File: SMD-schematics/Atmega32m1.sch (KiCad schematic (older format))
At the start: 33 parts, among them J11 Conn_02x06_Odd_Even, J12 Conn_02x06_Odd_Even, J7 Conn_02x06_Odd_Even, J8 Conn_02x06_Odd_Even, J9 DB9_Female, SW1 SW_Push_Dual, SW2 SW_Push_Dual, SW3 SW_Push_Dual, U5 MAX232, Y2 16Mhz

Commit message: "placing the footprints in PCB design no trakes yet"
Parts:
- JP5: renamed from JP?; footprint (none) -> Pin_Headers:Pin_Header_Straight_1x02_Pitch2.54mm
- U2: renamed from U?; footprint TQFP32 -> Housings_QFP:TQFP-32_7x7mm_Pitch0.8mm
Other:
- moved on the sheet: C10, C12, C13, C14, U5
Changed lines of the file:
@@
 L MAX232 U5
 U 1 1 59EBF4CD
-P 8600 3350
-F 0 "U5" H 8500 4475 50  0000 R CNN
-F 1 "MAX232" H 8500 4400 50  0000 R CNN
-F 2 "Housings_SOIC:SOIC-16_3.9x9.9mm_Pitch1.27mm" H 8650 2300 50  0001 L CNN
-F 3 "" H 8600 3450 50  0001 C CNN
-	1    8600 3350
+P 8450 3400
+F 0 "U5" H 8350 4525 50  0000 R CNN
+F 1 "MAX232" H 8350 4450 50  0000 R CNN
+F 2 "Housings_SOIC:SOIC-16_3.9x9.9mm_Pitch1.27mm" H 8500 2350 50  0001 L CNN
+F 3 "" H 8450 3500 50  0001 C CNN
+	1    8450 3400
 	1    0    0    -1
 $EndComp
@@
 L CP C10
 U 1 1 59EBFD51
-P 7350 2850
-F 0 "C10" H 7375 2950 50  0000 L CNN
-F 1 "1uf" H 7375 2750 50  0000 L CNN
-F 2 "Capacitors_SMD:CP_Elec_8x6.5" H 7388 2700 50  0001 C CNN
-F 3 "" H 7350 2850 50  0001 C CNN
-	1    7350 2850
+P 7350 2650
+F 0 "C10" H 7375 2750 50  0000 L CNN
+F 1 "1uf" H 7375 2550 50  0000 L CNN
+F 2 "Capacitors_SMD:CP_Elec_8x6.5" H 7388 2500 50  0001 C CNN
+F 3 "" H 7350 2650 50  0001 C CNN
+	1    7350 2650
 	1    0    0    -1
 $EndComp
@@
 L CP C12
 U 1 1 59EBFDFB
-P 9700 2850
-F 0 "C12" H 9725 2950 50  0000 L CNN
-F 1 "1uf" H 9725 2750 50  0000 L CNN
-F 2 "Capacitors_SMD:CP_Elec_8x6.5" H 9738 2700 50  0001 C CNN
-F 3 "" H 9700 2850 50  0001 C CNN
-	1    9700 2850
+P 9700 2650
+F 0 "C12" H 9725 2750 50  0000 L CNN
+F 1 "1uf" H 9725 2550 50  0000 L CNN
+F 2 "Capacitors_SMD:CP_Elec_8x6.5" H 9738 2500 50  0001 C CNN
+F 3 "" H 9700 2650 50  0001 C CNN
+	1    9700 2650
 	1    0    0    -1
 $EndComp
@@
 $EndComp
 $Comp
-L GND #PWR016
+L GND #PWR27
 U 1 1 59EBFEF1
 P 8650 2350
-F 0 "#PWR016" H 8650 2100 50  0001 C CNN
+F 0 "#PWR27" H 8650 2100 50  0001 C CNN
 F 1 "GND" H 8650 2200 50  0000 C CNN
 F 2 "" H 8650 2350 50  0001 C CNN
@@
 L CP C13
 U 1 1 59EBFF32
-P 10200 3200
-F 0 "C13" H 10225 3300 50  0000 L CNN
-F 1 "1uf" H 10225 3100 50  0000 L CNN
-F 2 "Capacitors_SMD:CP_Elec_8x6.5" H 10238 3050 50  0001 C CNN
-F 3 "" H 10200 3200 50  0001 C CNN
-	1    10200 3200
+P 10200 3000
+F 0 "C13" H 10225 3100 50  0000 L CNN
+F 1 "1uf" H 10225 2900 50  0000 L CNN
+F 2 "Capacitors_SMD:CP_Elec_8x6.5" H 10238 2850 50  0001 C CNN
+F 3 "" H 10200 3000 50  0001 C CNN
+	1    10200 3000
 	0    -1   -1   0
 $EndComp
@@
 L CP C14
 U 1 1 59EBFFAC
-P 10350 3550
-F 0 "C14" H 10375 3650 50  0000 L CNN
-F 1 "1uf" H 10375 3450 50  0000 L CNN
-F 2 "Capacitors_SMD:CP_Elec_8x6.5" H 10388 3400 50  0001 C CNN
-F 3 "" H 10350 3550 50  0001 C CNN
-	1    10350 3550
+P 10350 3350
+F 0 "C14" H 10375 3450 50  0000 L CNN
+F 1 "1uf" H 10375 3250 50  0000 L CNN
+F 2 "Capacitors_SMD:CP_Elec_8x6.5" H 10388 3200 50  0001 C CNN
+F 3 "" H 10350 3350 50  0001 C CNN
+	1    10350 3350
 	0    1    1    0
 $EndComp
 $Comp
-L GND #PWR017
+L GND #PWR28
 U 1 1 59EBFFE3
-P 10650 3350
-F 0 "#PWR017" H 10650 3100 50  0001 C CNN
-F 1 "GND" H 10650 3200 50  0000 C CNN
-F 2 "" H 10650 3350 50  0001 C CNN
-F 3 "" H 10650 3350 50  0001 C CNN
-	1    10650 3350
+P 10650 3150
+F 0 "#PWR28" H 10650 2900 50  0001 C CNN
+F 1 "GND" H 10650 3000 50  0000 C CNN
+F 2 "" H 10650 3150 50  0001 C CNN
+F 3 "" H 10650 3150 50  0001 C CNN
+	1    10650 3150
 	0    -1   -1   0
 $EndComp
 $Comp
-L GND #PWR018
+L GND #PWR26
 U 1 1 59EC0239
 P 8450 4950
-F 0 "#PWR018" H 8450 4700 50  0001 C CNN
+F 0 "#PWR26" H 8450 4700 50  0001 C CNN
 F 1 "GND" H 8450 4800 50  0000 C CNN
 F 2 "" H 8450 4950 50  0001 C CNN
@@
 $EndComp
 $Comp
-L +5V #PWR019
+L +5V #PWR17
 U 1 1 59EC0C0E
 P 4100 4200
-F 0 "#PWR019" H 4100 4050 50  0001 C CNN
+F 0 "#PWR17" H 4100 4050 50  0001 C CNN
 F 1 "+5V" H 4100 4340 50  0000 C CNN
 F 2 "" H 4100 4200 50  0001 C CNN
@@
 NoConn ~ 10350 5000
 $Comp
-L GND #PWR020
+L GND #PWR18
 U 1 1 5AA2B4DD
 P 4950 4850
-F 0 "#PWR020" H 4950 4600 50  0001 C CNN
+F 0 "#PWR18" H 4950 4600 50  0001 C CNN
 F 1 "GND" H 4950 4700 50  0000 C CNN
 F 2 "" H 4950 4850 50  0001 C CNN
@@
 $EndComp
 $Comp
-L GND #PWR021
+L GND #PWR13
 U 1 1 5AA312D5
 P 700 2150
-F 0 "#PWR021" H 700 1900 50  0001 C CNN
+F 0 "#PWR13" H 700 1900 50  0001 C CNN
 F 1 "GND" H 700 2000 50  0000 C CNN
 F 2 "" H 700 2150 50  0001 C CNN
@@
 $EndComp
 $Comp
-L +5V #PWR022
+L +5V #PWR14
 U 1 1 5AA3500F
 P 850 1250
-F 0 "#PWR022" H 850 1100 50  0001 C CNN
+F 0 "#PWR14" H 850 1100 50  0001 C CNN
 F 1 "+5V" H 850 1390 50  0000 C CNN
 F 2 "" H 850 1250 50  0001 C CNN
@@
 $EndComp
 $Comp
-L GND #PWR023
+L GND #PWR16
 U 1 1 5AA38656
 P 3550 6450
-F 0 "#PWR023" H 3550 6200 50  0001 C CNN
+F 0 "#PWR16" H 3550 6200 50  0001 C CNN
 F 1 "GND" H 3550 6300 50  0000 C CNN
 F 2 "" H 3550 6450 50  0001 C CNN
@@
 $EndComp
 $Comp
-L GND #PWR024
+L GND #PWR15
 U 1 1 5AA3A648
 P 850 4250
-F 0 "#PWR024" H 850 4000 50  0001 C CNN
+F 0 "#PWR15" H 850 4000 50  0001 C CNN
 F 1 "GND" H 850 4100 50  0000 C CNN
 F 2 "" H 850 4250 50  0001 C CNN
@@
 $EndComp
 $Comp
-L +5V #PWR025
+L +5V #PWR19
 U 1 1 5AA5B656
 P 5200 7350
-F 0 "#PWR025" H 5200 7200 50  0001 C CNN
+F 0 "#PWR19" H 5200 7200 50  0001 C CNN
 F 1 "+5V" H 5200 7490 50  0000 C CNN
 F 2 "" H 5200 7350 50  0001 C CNN
@@
 $EndComp
 $Comp
-L +5V #PWR026
+L +5V #PWR22
 U 1 1 5AA5B65C
 P 6000 4150
-F 0 "#PWR026" H 6000 4000 50  0001 C CNN
+F 0 "#PWR22" H 6000 4000 50  0001 C CNN
 F 1 "+5V" H 6000 4290 50  0000 C CNN
 F 2 "" H 6000 4150 50  0001 C CNN
@@
 AT-ADC2
 $Comp
-L GND #PWR027
+L GND #PWR20
 U 1 1 5AA5B91B
 P 5800 5250
-F 0 "#PWR027" H 5800 5000 50  0001 C CNN
+F 0 "#PWR20" H 5800 5000 50  0001 C CNN
 F 1 "GND" H 5800 5100 50  0000 C CNN
 F 2 "" H 5800 5250 50  0001 C CNN
@@
 $EndComp
 $Comp
-L +5V #PWR028
+L +5V #PWR25
 U 1 1 5AA5D9AA
 P 6900 4150
-F 0 "#PWR028" H 6900 4000 50  0001 C CNN
+F 0 "#PWR25" H 6900 4000 50  0001 C CNN
 F 1 "+5V" H 6900 4290 50  0000 C CNN
 F 2 "" H 6900 4150 50  0001 C CNN
@@
 AT-ADC3
 $Comp
-L GND #PWR029
+L GND #PWR21
 U 1 1 5AA6CC67
 P 5950 2900
-F 0 "#PWR029" H 5950 2650 50  0001 C CNN
+F 0 "#PWR21" H 5950 2650 50  0001 C CNN
 F 1 "GND" H 5950 2750 50  0000 C CNN
 F 2 "" H 5950 2900 50  0001 C CNN
@@
 $EndComp
 $Comp
-L GND #PWR030
+L GND #PWR23
 U 1 1 5AA87097
 P 6150 7350
-F 0 "#PWR030" H 6150 7100 50  0001 C CNN
+F 0 "#PWR23" H 6150 7100 50  0001 C CNN
 F 1 "GND" H 6150 7200 50  0000 C CNN
 F 2 "" H 6150 7350 50  0001 C CNN
@@
 $EndComp
 $Comp
-L GND #PWR031
+L GND #PWR24
 U 1 1 5AA88971
 P 6150 7600
-F 0 "#PWR031" H 6150 7350 50  0001 C CNN
+F 0 "#PWR24" H 6150 7350 50  0001 C CNN
 F 1 "GND" H 6150 7450 50  0000 C CNN
 F 2 "" H 6150 7600 50  0001 C CNN
@@
 	8650 2300 8650 2350
 Wire Wire Line
-	9550 3550 10200 3550
-Wire Wire Line
-	9250 3200 10050 3200
-Wire Wire Line
-	10550 3200 10350 3200
-Wire Wire Line
-	10550 3200 10550 3550
-Wire Wire Line
-	10550 3350 10650 3350
-Wire Wire Line
-	10550 3550 10500 3550
-Connection ~ 10550 3350
-Wire Wire Line
-	9250 2700 9700 2700
-Wire Wire Line
-	9700 3000 9250 3000
-Wire Wire Line
-	7650 2700 7350 2700
-Wire Wire Line
-	7350 3000 7650 3000
-Wire Wire Line
-	9550 3550 9550 3500
-Wire Wire Line
-	9550 3500 9250 3500
-Wire Wire Line
-	8450 4800 8450 4950
+	9550 3350 10200 3350
+Wire Wire Line
+	9250 3000 10050 3000
+Wire Wire Line
+	10550 3000 10350 3000
+Wire Wire Line
+	10550 3000 10550 3350
+Wire Wire Line
+	10550 3150 10650 3150
+Wire Wire Line
+	10550 3350 10500 3350
+Connection ~ 10550 3150
+Wire Wire Line
+	9250 2500 9700 2500
+Wire Wire Line
+	9700 2800 9250 2800
+Wire Wire Line
+	7650 2500 7350 2500
+Wire Wire Line
+	7350 2800 7650 2800
+Wire Wire Line
+	9550 3350 9550 3300
+Wire Wire Line
+	9550 3300 9250 3300
 Wire Wire Line
 	10350 4500 9750 4500
@@
 Wire Wire Line
 	9350 4850 8450 4850
-Connection ~ 8450 4850
 Wire Wire Line
 	4950 4850 4850 4850
@@
 ~AT-RST
 $Comp
-L ATMEGA32M1-AU U?
+L ATMEGA32M1-AU U2
 U 1 1 5AC2CAD1
 P 2350 3100
-F 0 "U?" H 1400 4930 50  0000 L BNN
+F 0 "U2" H 1400 4930 50  0000 L BNN
 F 1 "ATMEGA32M1-AU" H 2850 1700 50  0000 L BNN
-F 2 "TQFP32" H 2350 3100 50  0001 C CIN
+F 2 "Housings_QFP:TQFP-32_7x7mm_Pitch0.8mm" H 2350 3100 50  0001 C CIN
 F 3 "" H 2350 3100 50  0001 C CNN
 	1    2350 3100
@@
 SPI-DW
 $Comp
-L Jumper_NO_Small JP?
+L Jumper_NO_Small JP5
 U 1 1 5AC326E0
 P 10650 1850
-F 0 "JP?" H 10650 1930 50  0000 C CNN
+F 0 "JP5" H 10650 1930 50  0000 C CNN
 F 1 "Jumper_NO_Small" H 10660 1790 50  0000 C CNN
-F 2 "" H 10650 1850 50  0001 C CNN
+F 2 "Pin_Headers:Pin_Header_Straight_1x02_Pitch2.54mm" H 10650 1850 50  0001 C CNN
 F 3 "" H 10650 1850 50  0001 C CNN
 	1    10650 1850
@@
 Wire Wire Line
 	10400 1950 10650 1950
+Wire Wire Line
+	8450 4850 8450 4950
 $EndSCHEMATC

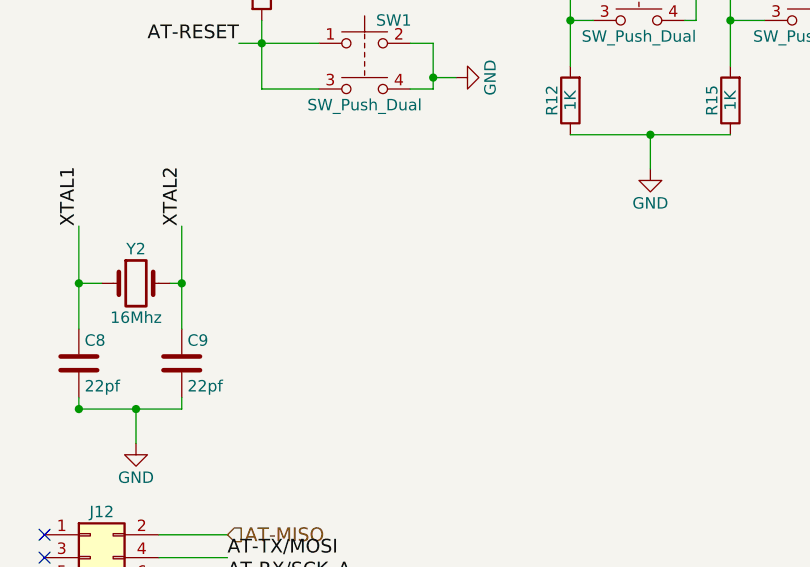
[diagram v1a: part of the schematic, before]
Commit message: updating schematics with pins for GND and VCC
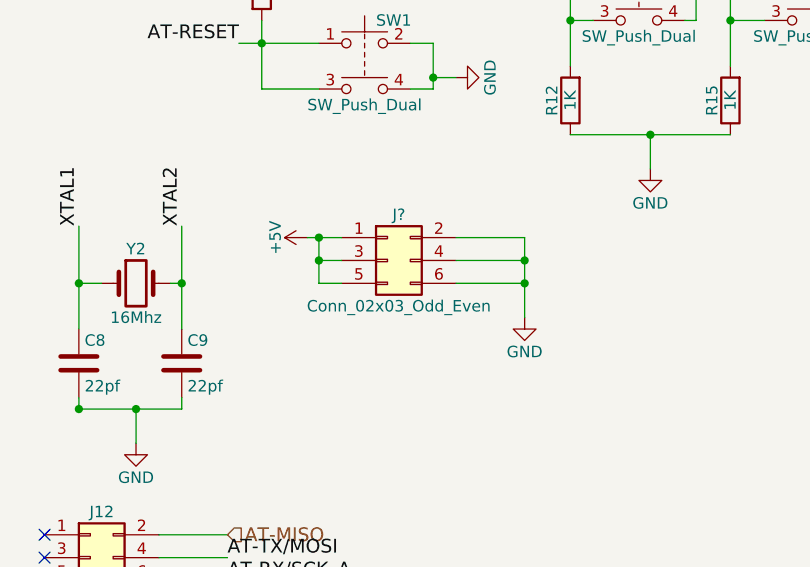
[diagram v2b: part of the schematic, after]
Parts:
- added J?: Conn_02x03_Odd_Even, symbol Conn_02x03_Odd_Even
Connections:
- net +5V: now also J?.1 (Pin_1), J?.3 (Pin_3), J?.5 (Pin_5)
- net GND: now also J?.2 (Pin_2), J?.4 (Pin_4), J?.6 (Pin_6)
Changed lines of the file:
@@
 Wire Wire Line
 	8450 4850 8450 4950
+$Comp
+L Conn_02x03_Odd_Even J?
+U 1 1 5AD2B36D
+P 4650 5650
+F 0 "J?" H 4700 5850 50  0000 C CNN
+F 1 "Conn_02x03_Odd_Even" H 4700 5450 50  0000 C CNN
+F 2 "" H 4650 5650 50  0001 C CNN
+F 3 "" H 4650 5650 50  0001 C CNN
+	1    4650 5650
+	1    0    0    -1
+$EndComp
+$Comp
+L +5V #PWR?
+U 1 1 5AD2B551
+P 4300 5550
+F 0 "#PWR?" H 4300 5400 50  0001 C CNN
+F 1 "+5V" H 4300 5690 50  0000 C CNN
+F 2 "" H 4300 5550 50  0001 C CNN
+F 3 "" H 4300 5550 50  0001 C CNN
+	1    4300 5550
+	0    -1   -1   0
+$EndComp
+Wire Wire Line
+	4450 5550 4300 5550
+Wire Wire Line
+	4450 5650 4350 5650
+Wire Wire Line
+	4350 5550 4350 5750
+Connection ~ 4350 5550
+Wire Wire Line
+	4350 5750 4450 5750
+Connection ~ 4350 5650
+$Comp
+L GND #PWR?
+U 1 1 5AD2B9E2
+P 5250 5900
+F 0 "#PWR?" H 5250 5650 50  0001 C CNN
+F 1 "GND" H 5250 5750 50  0000 C CNN
+F 2 "" H 5250 5900 50  0001 C CNN
+F 3 "" H 5250 5900 50  0001 C CNN
+	1    5250 5900
+	1    0    0    -1
+$EndComp
+Wire Wire Line
+	4950 5550 5250 5550
+Wire Wire Line
+	5250 5550 5250 5900
+Wire Wire Line
+	4950 5650 5250 5650
+Connection ~ 5250 5650
+Wire Wire Line
+	4950 5750 5250 5750
+Connection ~ 5250 5750
 $EndSCHEMATC

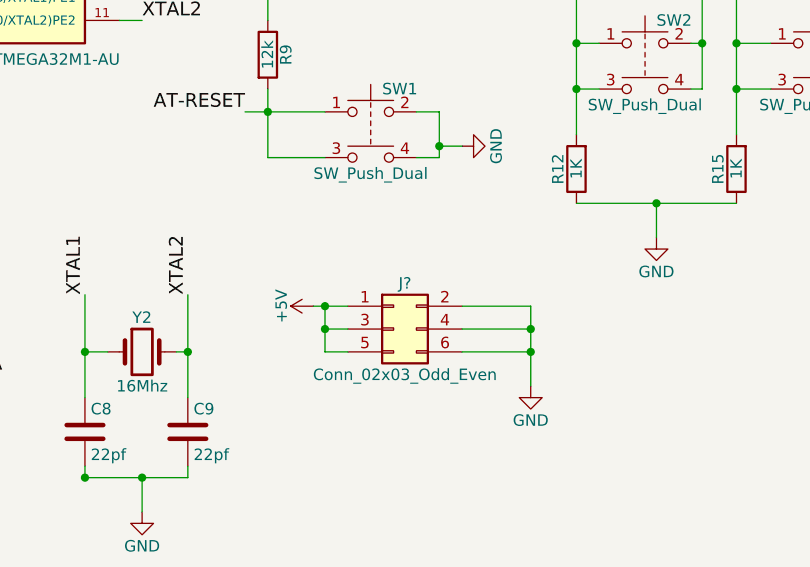
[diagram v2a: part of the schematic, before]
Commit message: "size of PCB 8*8 before tracking"
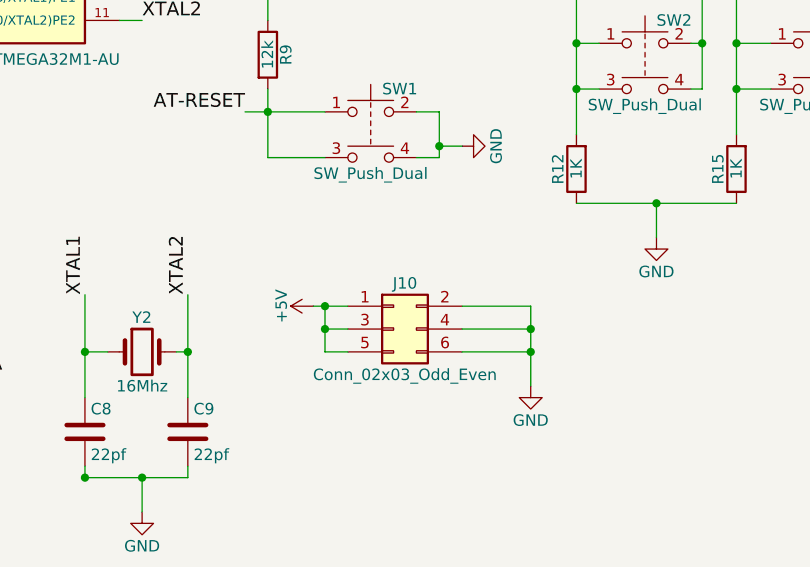
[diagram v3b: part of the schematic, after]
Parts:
- J10: renamed from J?; footprint (none) -> Pin_Headers:Pin_Header_Straight_2x03_Pitch2.54mm
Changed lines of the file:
@@
 $EndComp
 $Comp
-L GND #PWR27
+L GND #PWR016
 U 1 1 59EBFEF1
 P 8650 2350
-F 0 "#PWR27" H 8650 2100 50  0001 C CNN
+F 0 "#PWR016" H 8650 2100 50  0001 C CNN
 F 1 "GND" H 8650 2200 50  0000 C CNN
 F 2 "" H 8650 2350 50  0001 C CNN
@@
 $EndComp
 $Comp
-L GND #PWR28
+L GND #PWR017
 U 1 1 59EBFFE3
 P 10650 3150
-F 0 "#PWR28" H 10650 2900 50  0001 C CNN
+F 0 "#PWR017" H 10650 2900 50  0001 C CNN
 F 1 "GND" H 10650 3000 50  0000 C CNN
 F 2 "" H 10650 3150 50  0001 C CNN
@@
 $EndComp
 $Comp
-L GND #PWR26
+L GND #PWR018
 U 1 1 59EC0239
 P 8450 4950
-F 0 "#PWR26" H 8450 4700 50  0001 C CNN
+F 0 "#PWR018" H 8450 4700 50  0001 C CNN
 F 1 "GND" H 8450 4800 50  0000 C CNN
 F 2 "" H 8450 4950 50  0001 C CNN
@@
 $EndComp
 $Comp
-L +5V #PWR17
+L +5V #PWR019
 U 1 1 59EC0C0E
 P 4100 4200
-F 0 "#PWR17" H 4100 4050 50  0001 C CNN
+F 0 "#PWR019" H 4100 4050 50  0001 C CNN
 F 1 "+5V" H 4100 4340 50  0000 C CNN
 F 2 "" H 4100 4200 50  0001 C CNN
@@
 NoConn ~ 10350 5000
 $Comp
-L GND #PWR18
+L GND #PWR020
 U 1 1 5AA2B4DD
 P 4950 4850
-F 0 "#PWR18" H 4950 4600 50  0001 C CNN
+F 0 "#PWR020" H 4950 4600 50  0001 C CNN
 F 1 "GND" H 4950 4700 50  0000 C CNN
 F 2 "" H 4950 4850 50  0001 C CNN
@@
 $EndComp
 $Comp
-L GND #PWR13
+L GND #PWR021
 U 1 1 5AA312D5
 P 700 2150
-F 0 "#PWR13" H 700 1900 50  0001 C CNN
+F 0 "#PWR021" H 700 1900 50  0001 C CNN
 F 1 "GND" H 700 2000 50  0000 C CNN
 F 2 "" H 700 2150 50  0001 C CNN
@@
 $EndComp
 $Comp
-L +5V #PWR14
+L +5V #PWR022
 U 1 1 5AA3500F
 P 850 1250
-F 0 "#PWR14" H 850 1100 50  0001 C CNN
+F 0 "#PWR022" H 850 1100 50  0001 C CNN
 F 1 "+5V" H 850 1390 50  0000 C CNN
 F 2 "" H 850 1250 50  0001 C CNN
@@
 $EndComp
 $Comp
-L GND #PWR16
+L GND #PWR023
 U 1 1 5AA38656
 P 3550 6450
-F 0 "#PWR16" H 3550 6200 50  0001 C CNN
+F 0 "#PWR023" H 3550 6200 50  0001 C CNN
 F 1 "GND" H 3550 6300 50  0000 C CNN
 F 2 "" H 3550 6450 50  0001 C CNN
@@
 $EndComp
 $Comp
-L GND #PWR15
+L GND #PWR024
 U 1 1 5AA3A648
 P 850 4250
-F 0 "#PWR15" H 850 4000 50  0001 C CNN
+F 0 "#PWR024" H 850 4000 50  0001 C CNN
 F 1 "GND" H 850 4100 50  0000 C CNN
 F 2 "" H 850 4250 50  0001 C CNN
@@
 $EndComp
 $Comp
-L +5V #PWR19
+L +5V #PWR025
 U 1 1 5AA5B656
 P 5200 7350
-F 0 "#PWR19" H 5200 7200 50  0001 C CNN
+F 0 "#PWR025" H 5200 7200 50  0001 C CNN
 F 1 "+5V" H 5200 7490 50  0000 C CNN
 F 2 "" H 5200 7350 50  0001 C CNN
@@
 $EndComp
 $Comp
-L +5V #PWR22
+L +5V #PWR026
 U 1 1 5AA5B65C
 P 6000 4150
-F 0 "#PWR22" H 6000 4000 50  0001 C CNN
+F 0 "#PWR026" H 6000 4000 50  0001 C CNN
 F 1 "+5V" H 6000 4290 50  0000 C CNN
 F 2 "" H 6000 4150 50  0001 C CNN
@@
 AT-ADC2
 $Comp
-L GND #PWR20
+L GND #PWR027
 U 1 1 5AA5B91B
 P 5800 5250
-F 0 "#PWR20" H 5800 5000 50  0001 C CNN
+F 0 "#PWR027" H 5800 5000 50  0001 C CNN
 F 1 "GND" H 5800 5100 50  0000 C CNN
 F 2 "" H 5800 5250 50  0001 C CNN
@@
 $EndComp
 $Comp
-L +5V #PWR25
+L +5V #PWR028
 U 1 1 5AA5D9AA
 P 6900 4150
-F 0 "#PWR25" H 6900 4000 50  0001 C CNN
+F 0 "#PWR028" H 6900 4000 50  0001 C CNN
 F 1 "+5V" H 6900 4290 50  0000 C CNN
 F 2 "" H 6900 4150 50  0001 C CNN
@@
 AT-ADC3
 $Comp
-L GND #PWR21
+L GND #PWR029
 U 1 1 5AA6CC67
 P 5950 2900
-F 0 "#PWR21" H 5950 2650 50  0001 C CNN
+F 0 "#PWR029" H 5950 2650 50  0001 C CNN
 F 1 "GND" H 5950 2750 50  0000 C CNN
 F 2 "" H 5950 2900 50  0001 C CNN
@@
 $EndComp
 $Comp
-L GND #PWR23
+L GND #PWR030
 U 1 1 5AA87097
 P 6150 7350
-F 0 "#PWR23" H 6150 7100 50  0001 C CNN
+F 0 "#PWR030" H 6150 7100 50  0001 C CNN
 F 1 "GND" H 6150 7200 50  0000 C CNN
 F 2 "" H 6150 7350 50  0001 C CNN
@@
 $EndComp
 $Comp
-L GND #PWR24
+L GND #PWR031
 U 1 1 5AA88971
 P 6150 7600
-F 0 "#PWR24" H 6150 7350 50  0001 C CNN
+F 0 "#PWR031" H 6150 7350 50  0001 C CNN
 F 1 "GND" H 6150 7450 50  0000 C CNN
 F 2 "" H 6150 7600 50  0001 C CNN
@@
 	8450 4850 8450 4950
 $Comp
-L Conn_02x03_Odd_Even J?
+L Conn_02x03_Odd_Even J10
 U 1 1 5AD2B36D
 P 4650 5650
-F 0 "J?" H 4700 5850 50  0000 C CNN
+F 0 "J10" H 4700 5850 50  0000 C CNN
 F 1 "Conn_02x03_Odd_Even" H 4700 5450 50  0000 C CNN
-F 2 "" H 4650 5650 50  0001 C CNN
+F 2 "Pin_Headers:Pin_Header_Straight_2x03_Pitch2.54mm" H 4650 5650 50  0001 C CNN
 F 3 "" H 4650 5650 50  0001 C CNN
 	1    4650 5650
@@
 $EndComp
 $Comp
-L +5V #PWR?
+L +5V #PWR032
 U 1 1 5AD2B551
 P 4300 5550
-F 0 "#PWR?" H 4300 5400 50  0001 C CNN
+F 0 "#PWR032" H 4300 5400 50  0001 C CNN
 F 1 "+5V" H 4300 5690 50  0000 C CNN
 F 2 "" H 4300 5550 50  0001 C CNN
@@
 Connection ~ 4350 5650
 $Comp
-L GND #PWR?
+L GND #PWR033
 U 1 1 5AD2B9E2
 P 5250 5900
-F 0 "#PWR?" H 5250 5650 50  0001 C CNN
+F 0 "#PWR033" H 5250 5650 50  0001 C CNN
 F 1 "GND" H 5250 5750 50  0000 C CNN
 F 2 "" H 5250 5900 50  0001 C CNN
